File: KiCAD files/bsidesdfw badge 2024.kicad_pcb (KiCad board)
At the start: 2 copper layers, 117.4 x 117.4 mm, 29 parts, among them Q1 BC548, SW1 SW_SPDT_312, U1 NE555P, U2 74HC595

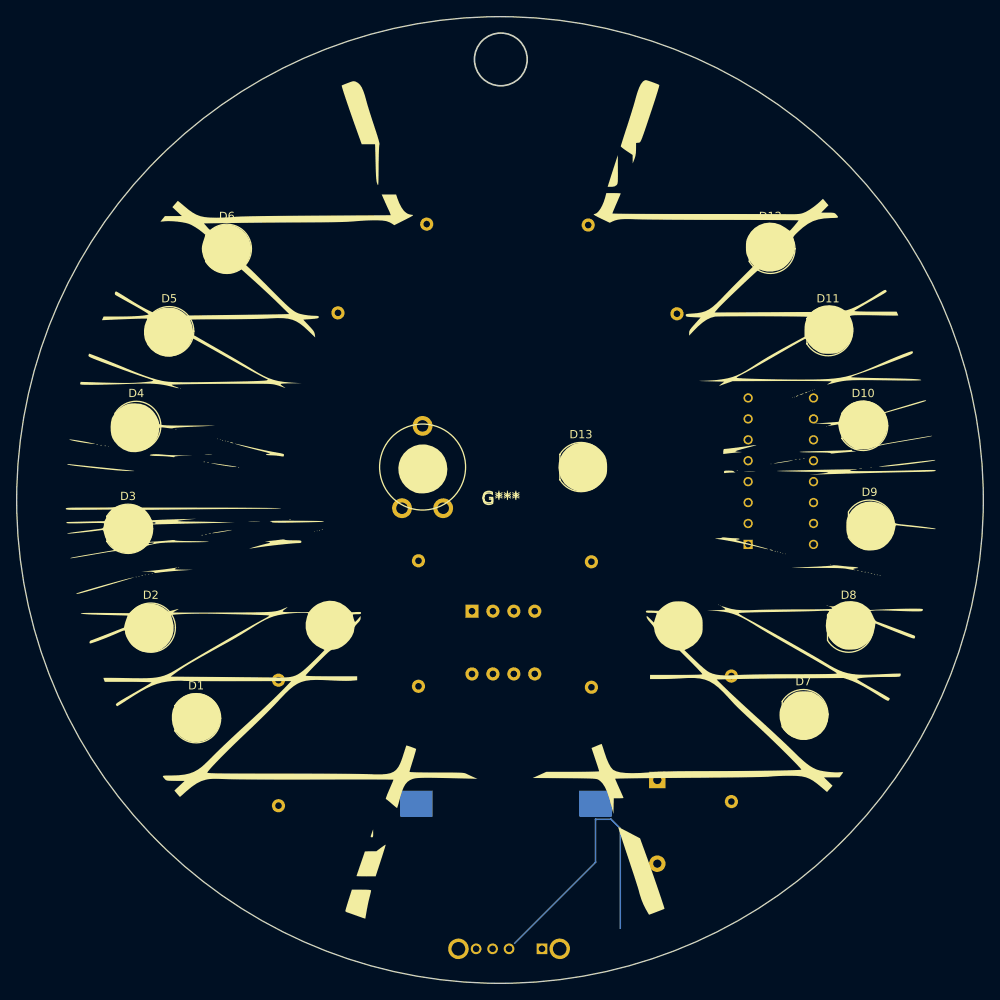
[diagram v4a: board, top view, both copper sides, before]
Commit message: trace rerouting; some silkscreen cleanup. Need to remake the aesthetic mask to fix the dots overlapping the LEDs
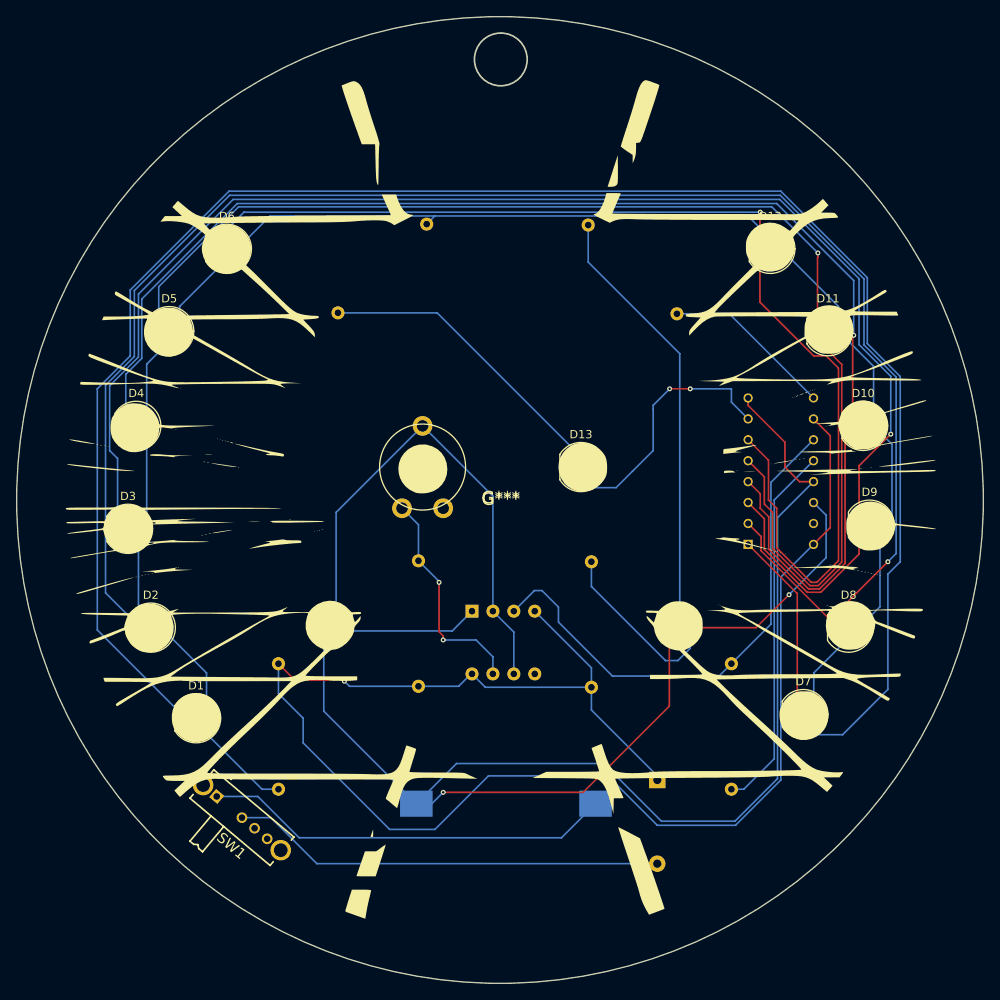
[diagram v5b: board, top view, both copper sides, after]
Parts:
- SW1: moved to F.Cu
- moved SW1 43.6 mm to (103.0, 132.5), turned to -40 degrees
- moved R6 2.00 mm to (110.5, 131.6)
- moved R5 1.50 mm to (165.5, 131.6)
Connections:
- D13 pad 1: Net-(D1-K) -> Net-(D13-K)
- D4 pad 1: Net-(D4-K) -> Net-(D10-K)
- D5 pad 1: Net-(D10-K) -> Net-(D11-K)
- D6 pad 1: Net-(D11-K) -> Net-(D12-K)
- D7 pad 1: Net-(D2-K) -> Net-(D1-K)
- D8 pad 1: Net-(D3-K) -> Net-(D2-K)
- D9 pad 1: Net-(D4-K) -> Net-(D3-K)
- SW1 pad 1: Net-(D14-A) -> Net-(BT1-+)
- SW1 pad 2: Net-(BT1-+) -> Net-(D14-A)
- U2 pad 1: Net-(D2-K) -> Net-(D1-K)
- U2 pad 15: Net-(D1-K) -> unconnected-(U2-QA-Pad15)
- U2 pad 2: Net-(D3-K) -> Net-(D2-K)
- U2 pad 3: Net-(D4-K) -> Net-(D3-K)
- U2 pad 7: unconnected-(U2-QH-Pad7) -> Net-(D13-K)
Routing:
- net Net-(D1-K): track 0.00 -> 248.2 mm
- net Net-(D1-A): track 0.00 -> 215.8 mm
- net Net-(D2-K): track 0.00 -> 205.8 mm, vias 0 -> 1
- net +6V: track 0.00 -> 194.9 mm, vias 0 -> 1
- net GND: track 0.00 -> 194.8 mm, vias 0 -> 1
- net Net-(D3-K): track 0.00 -> 185.3 mm, vias 0 -> 1
- net Net-(D10-K): track 0.00 -> 167.9 mm, vias 0 -> 1
- net Net-(D11-K): track 0.00 -> 153.9 mm, vias 0 -> 1
- net Net-(D12-K): track 0.00 -> 140.6 mm, vias 0 -> 1
- net Net-(U1-Q): track 0.00 -> 64.8 mm
- net Net-(U1-THR): track 0.00 -> 63.1 mm
- net Net-(Q1-B): track 0.00 -> 53.5 mm
- net Net-(D14-A): track 0.00 -> 52.8 mm
- net Net-(BT1-+): track 0.00 -> 49.8 mm
- net Net-(Q1-C): track 0.00 -> 49.4 mm, vias 0 -> 1
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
